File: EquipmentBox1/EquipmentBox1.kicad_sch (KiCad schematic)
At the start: 11 parts, among them J1 UAC16-9, J10 UAV20-5, J11 UAC28-2, J2 UAC16-9, J3 UAC16-9, J4 UAC16-9, J5 UAC16-8, J6 UAC16-8, J7 UAC16-8, J8 UAC16-8, J9 UAV20-5

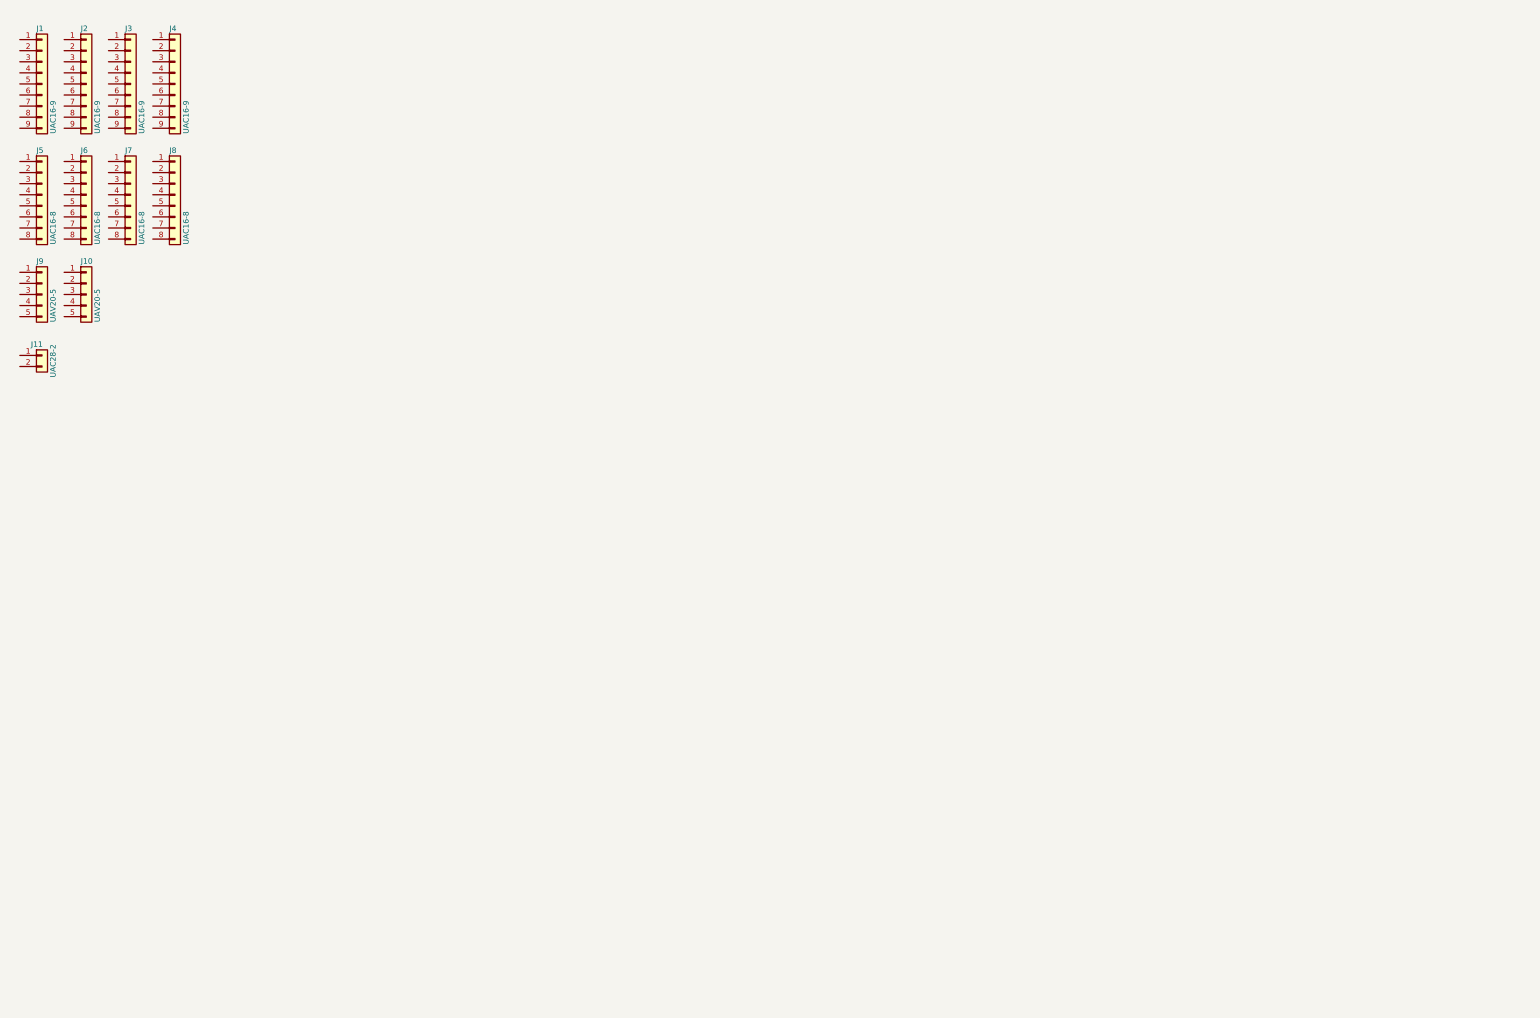
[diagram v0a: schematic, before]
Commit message: 已打样测试两版，第三版暂未修改
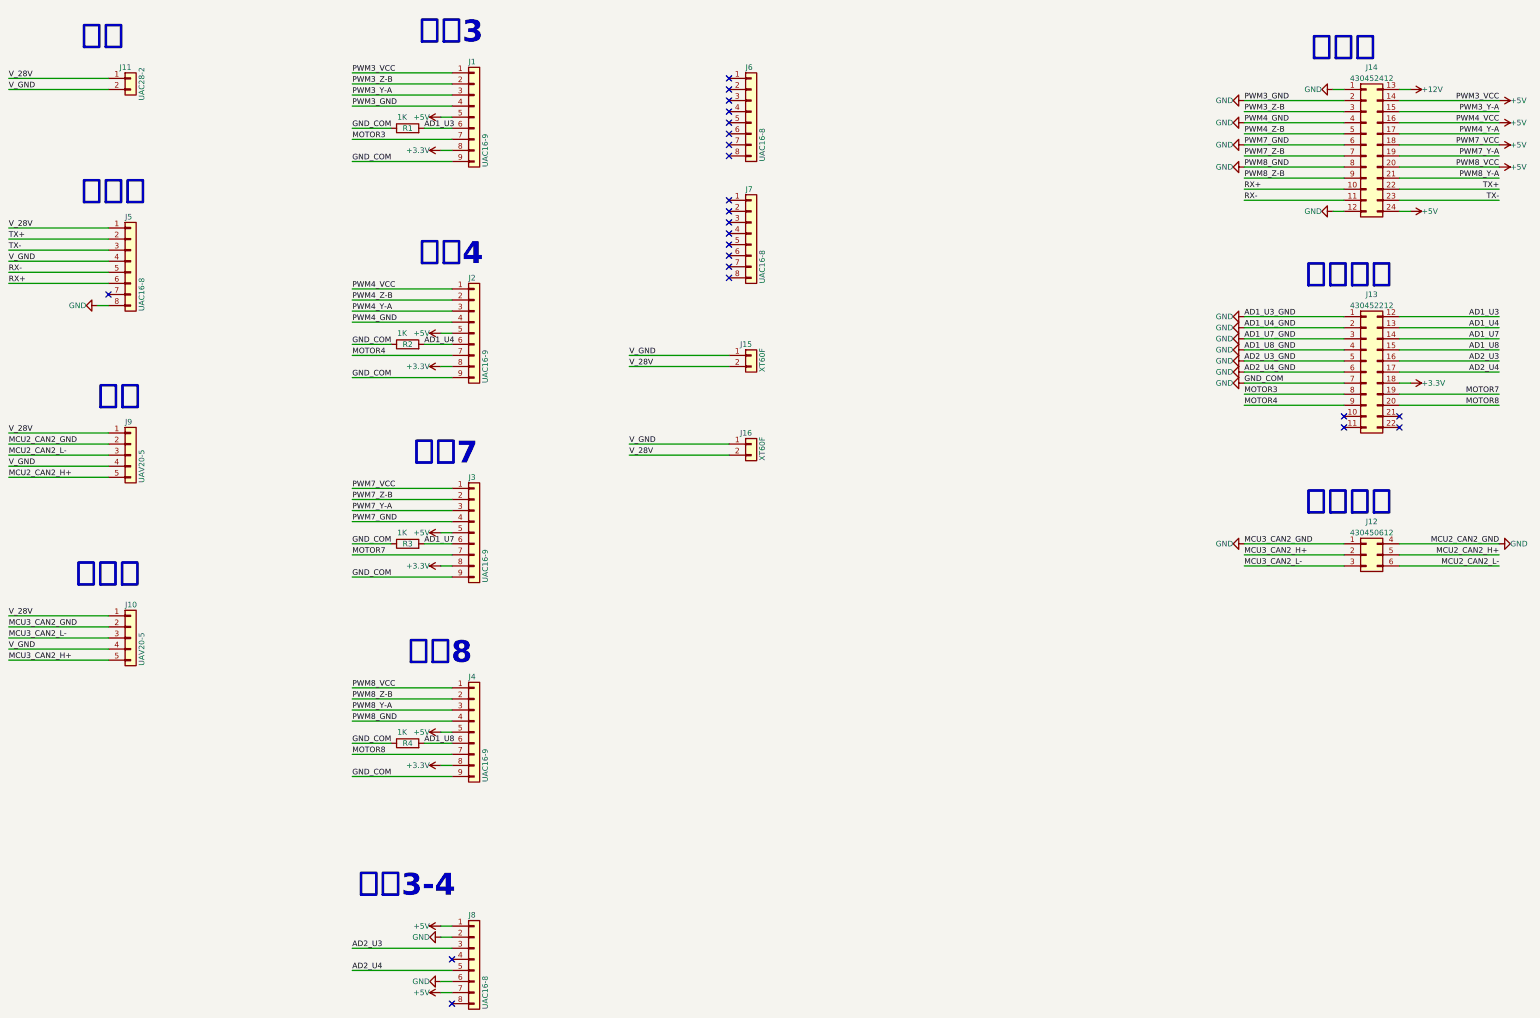
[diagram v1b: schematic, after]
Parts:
- added J12: 430450612, Molex:430450612, symbol Connector_Generic:Conn_02x03_Top_Bottom
- added J13: 430452212, Molex:430452212, symbol Connector_Generic:Conn_02x11_Top_Bottom
- added J14: 430452412, Molex:430452412, symbol Connector_Generic:Conn_02x12_Top_Bottom
- added J15, J16: XT60F, Connector_AMASS:AMASS_XT60-F_1x02_P7.20mm_Vertical, symbol Connector_Generic:Conn_01x02
- added R1, R2, R3, R4: 1K, Resistor_SMD:R_0402_1005Metric, symbol Device:R
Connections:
- net V_28V: now reaches J9.1 (Pin_1)
- net V_28V: now also J10.1 (Pin_1), J11.1 (Pin_1), J5.1 (Pin_1), J15.2 (Pin_2), J16.2 (Pin_2)
- net GND: now reaches J9.2 (Pin_2)
- net GND: now also J1.4 (Pin_4), J1.9 (Pin_9), J10.2 (Pin_2), J2.4 (Pin_4), J2.9 (Pin_9), J3.4 (Pin_4), J3.9 (Pin_9), J4.4 (Pin_4), J4.9 (Pin_9), J5.8 (Pin_8), J8.2 (Pin_2), J8.6 (Pin_6), J12.1 (Pin_1), J12.4 (Pin_4), J13.1 (Pin_1), J13.2 (Pin_2), J13.3 (Pin_3), J13.4 (Pin_4), J13.5 (Pin_5), J13.6 (Pin_6), J13.7 (Pin_7), J14.1 (Pin_1), J14.12 (Pin_12), J14.2 (Pin_2), J14.4 (Pin_4), J14.6 (Pin_6), J14.8 (Pin_8), R1.1, R2.1, R3.1, R4.1
- net MCU2_CAN2_L-: now reaches J9.3 (Pin_3)
- net MCU2_CAN2_L-: now also J12.6 (Pin_6)
- net V_GND: now reaches J9.4 (Pin_4)
- net V_GND: now also J10.4 (Pin_4), J11.2 (Pin_2), J5.4 (Pin_4), J15.1 (Pin_1), J16.1 (Pin_1)
- net MCU2_CAN2_H+: now reaches J9.5 (Pin_5)
- net MCU2_CAN2_H+: now also J12.5 (Pin_5)
- net +5V: now reaches J4.1 (Pin_1)
- net +5V: now also J1.1 (Pin_1), J1.5 (Pin_5), J2.1 (Pin_1), J2.5 (Pin_5), J3.1 (Pin_1), J3.5 (Pin_5), J4.5 (Pin_5), J8.1 (Pin_1), J8.7 (Pin_7), J14.14 (Pin_14), J14.16 (Pin_16), J14.18 (Pin_18), J14.20 (Pin_20), J14.24 (Pin_24)
- net PWM8_Z-B: now reaches J4.2 (Pin_2)
- net PWM8_Z-B: now also J14.9 (Pin_9)
- net PWM8_Y-A: now reaches J4.3 (Pin_3)
- net PWM8_Y-A: now also J14.21 (Pin_21)
- net AD1_U8: now reaches J4.6 (Pin_6)
- net AD1_U8: now also J13.15 (Pin_15), R4.2
- net MOTOR8: now reaches J4.7 (Pin_7)
- net MOTOR8: now also J13.20 (Pin_20)
- net +3.3V: now reaches J4.8 (Pin_8)
- net +3.3V: now also J1.8 (Pin_8), J2.8 (Pin_8), J3.8 (Pin_8), J13.18 (Pin_18)
- net PWM3_Z-B: now reaches J1.2 (Pin_2)
- net PWM3_Z-B: now also J14.3 (Pin_3)
- net PWM3_Y-A: now reaches J1.3 (Pin_3)
- net PWM3_Y-A: now also J14.15 (Pin_15)
- net AD1_U3: now reaches J1.6 (Pin_6)
- net AD1_U3: now also J13.12 (Pin_12), R1.2
- net MOTOR3: now reaches J1.7 (Pin_7)
- net MOTOR3: now also J13.8 (Pin_8)
- net PWM7_Z-B: now reaches J3.2 (Pin_2)
- net PWM7_Z-B: now also J14.7 (Pin_7)
- net PWM7_Y-A: now reaches J3.3 (Pin_3)
- net PWM7_Y-A: now also J14.19 (Pin_19)
- net AD1_U7: now reaches J3.6 (Pin_6)
- net AD1_U7: now also J13.14 (Pin_14), R3.2
- net MOTOR7: now reaches J3.7 (Pin_7)
- net MOTOR7: now also J13.19 (Pin_19)
- net PWM4_Z-B: now reaches J2.2 (Pin_2)
- net PWM4_Z-B: now also J14.5 (Pin_5)
- net PWM4_Y-A: now reaches J2.3 (Pin_3)
- net PWM4_Y-A: now also J14.17 (Pin_17)
- net AD1_U4: now reaches J2.6 (Pin_6)
- net AD1_U4: now also J13.13 (Pin_13), R2.2
- net MOTOR4: now reaches J2.7 (Pin_7)
- net MOTOR4: now also J13.9 (Pin_9)
- net MCU3_CAN2_L-: now reaches J10.3 (Pin_3)
- net MCU3_CAN2_L-: now also J12.3 (Pin_3)
- net MCU3_CAN2_H+: now reaches J10.5 (Pin_5)
- net MCU3_CAN2_H+: now also J12.2 (Pin_2)
- net AD2_U3: now reaches J8.3 (Pin_3)
- net AD2_U3: now also J13.16 (Pin_16)
- net AD2_U4: now reaches J8.5 (Pin_5)
- net AD2_U4: now also J13.17 (Pin_17)
- net TX+: now reaches J5.2 (Pin_2)
- net TX+: now also J14.22 (Pin_22)
- net TX-: now reaches J5.3 (Pin_3)
- net TX-: now also J14.23 (Pin_23)
- net RX-: now reaches J5.5 (Pin_5)
- net RX-: now also J14.11 (Pin_11)
- net RX+: now reaches J5.6 (Pin_6)
- net RX+: now also J14.10 (Pin_10)
- new net +12V: J14.13 (Pin_13)
- no-connect marks 0 -> 23
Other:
- note added: "倾转3-4"
- note added: "右机翼"
- note added: "大气机"
- note added: "尾翼"
- note added: "电源"
- note added: "电调3"
- note added: "电调4"
- note added: "电调7"
- note added: "电调8"
- note added: "转发板右"
- note added: "采集板右"
- note added: "飞控右"
- company: (none) -> 南京拓兴智控
- title: (none) -> 设备盒PCB1
- moved on the sheet: J1, J10, J11, J2, J3, J4, J5, J6, J7, J8, J9
